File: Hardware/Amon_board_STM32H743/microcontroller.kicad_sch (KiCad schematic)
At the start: 52 parts, among them J1 USB_C_Receptacle_USB2.0, J4 HAB-VCR-010-LF, SW3 SW_SPST, U14 CH340G, U3 W25Q128JVS, U9 STM32H743VIT6, Y1 48MHz, Y2 32.768kHz, Y5 12MHz

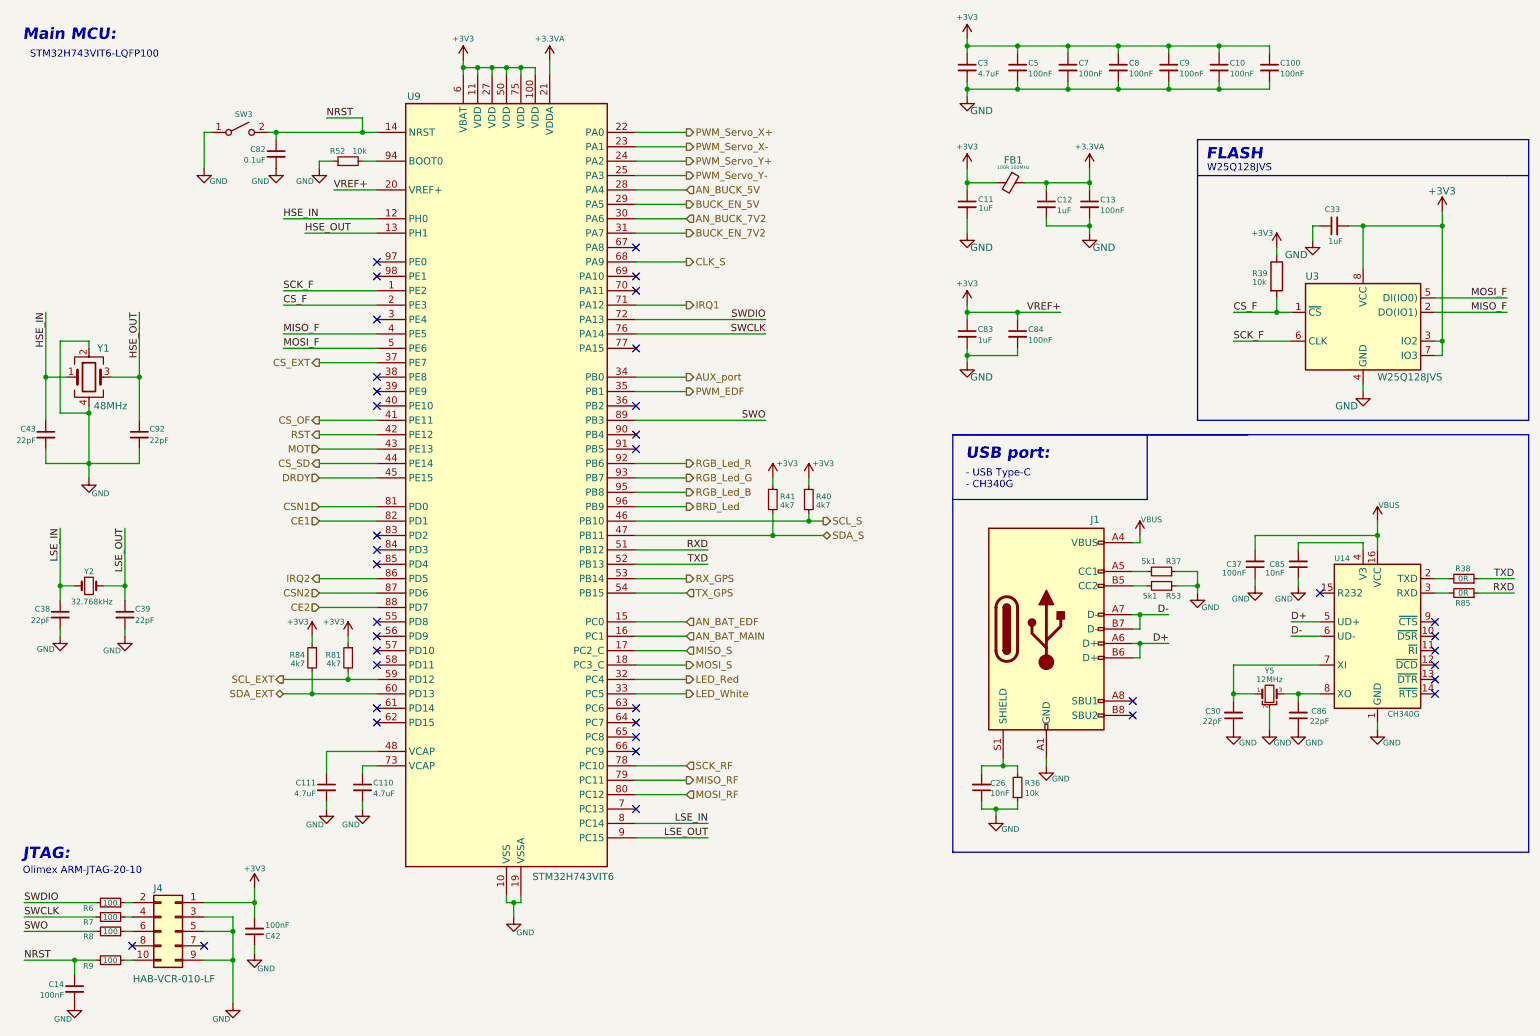
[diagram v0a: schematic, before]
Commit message: Update: finished PCB v3, gerbers, ordered board, readme update
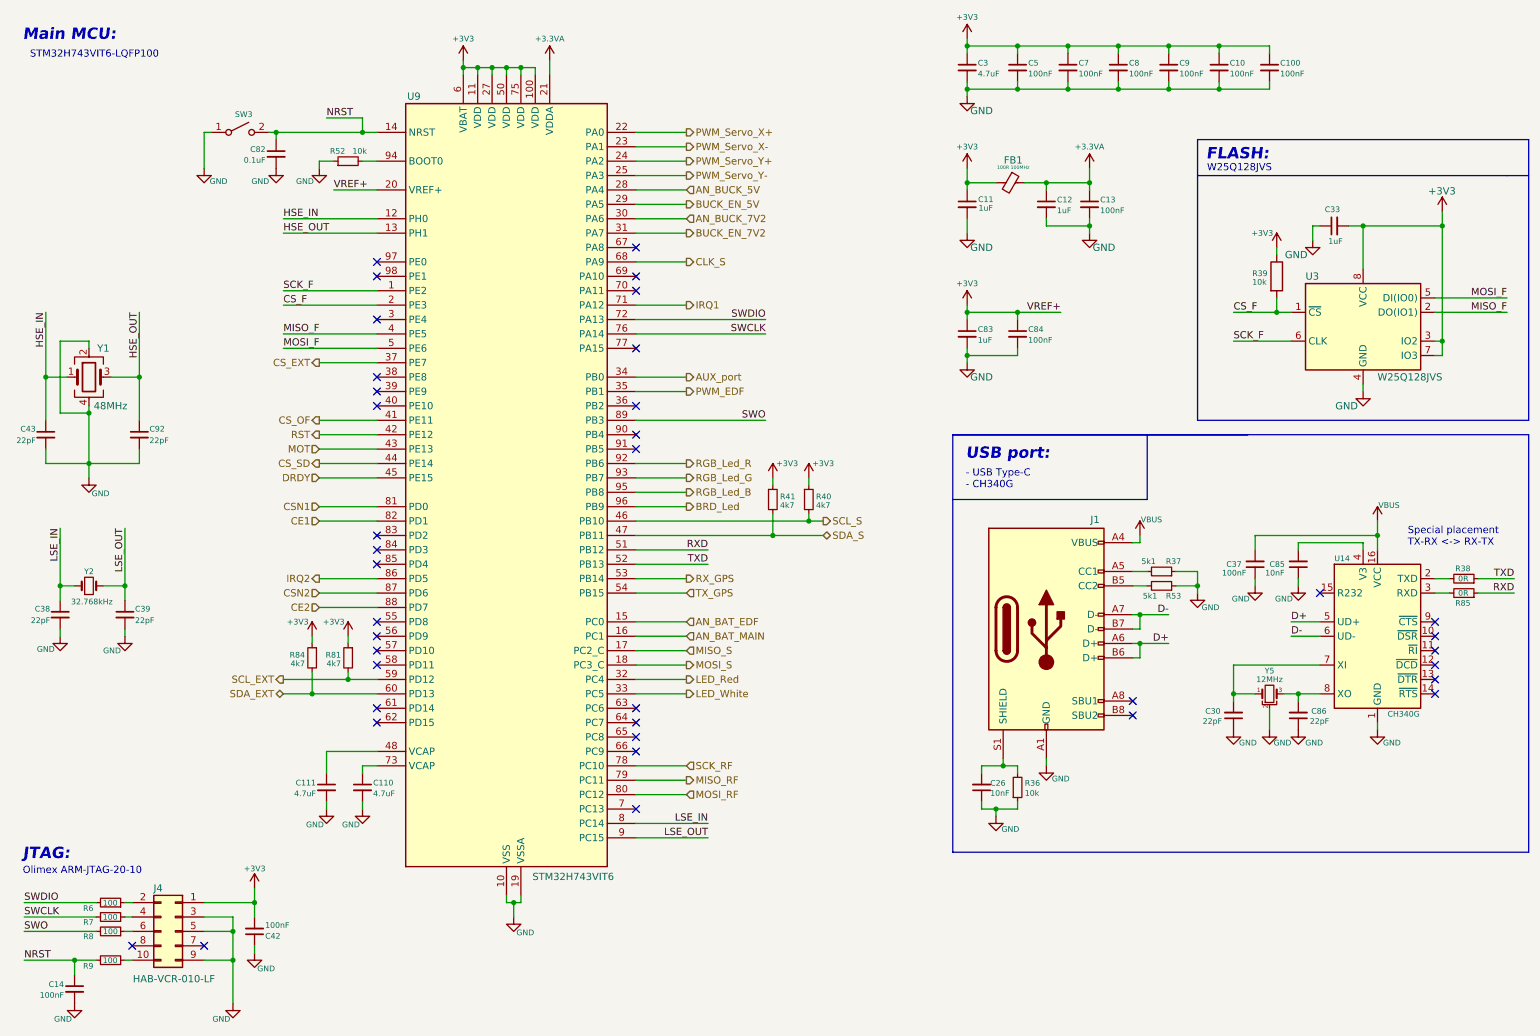
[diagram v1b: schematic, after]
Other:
- note added: "FLASH:"
- note added: "Special placement TX-RX <-> RX-TX"
- note removed: "FLASH"
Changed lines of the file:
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@@
 		)
 	)
-	(text "FLASH"
+	(text "FLASH:"
 		(exclude_from_sim no)
 		(at 226.314 41.91 0)
@@
 				(bold yes)
 				(italic yes)
+				(color 132 0 0 1)
 			)
 			(justify left bottom)
 		)
 	)
+	(text "Special placement\nTX-RX <-> RX-TX"
+		(exclude_from_sim no)
+		(at 261.874 109.982 0)
+		(effects
+			(font
+				(size 1.27 1.27)
+			)
+			(justify left bottom)
+		)
+	)
 	(junction
 		(at 35.56 116.84)
@@
 	(wire
 		(pts
-			(xy 67.31 54.61) (xy 80.01 54.61)
+			(xy 63.5 54.61) (xy 80.01 54.61)
 		)
 		(stroke
@@
 	)
 	(label "HSE_OUT"
-		(at 67.31 54.61 0)
+		(at 63.5 54.61 0)
 		(effects
 			(font
